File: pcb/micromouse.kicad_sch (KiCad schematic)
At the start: 41 parts, among them J1 B2B-PH-K-S, J12 PINHD_1x5_Female, J15 PINHD_1x2_Female, J2 B2B-PH-K-S, J3 B6B-ZR, J4 B6B-ZR, J7 PINHD_1x5_Female, M1 Left, M2 Right, SW2 SW_DIP_x04, U1 AZ1117-3.3, U2 L293DD, U3 STM32F411RETx, Y1 25 MHz 10 pF, Y2 32.768 kHz 7 pF

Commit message: Add files via upload
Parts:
- J13: renamed from J4; footprint CONN_B6B-ZR_JST -> B6B_ZR:CONN_B6B-ZR_JST
- renumbered C19 to C1, C17 to C10, C20 to C11, C16 to C12, C22 to C16, C5 to C17, C6 to C18, C3 to C19, C12 to C2, C4 to C20, C2 to C21, C1 to C22, C14 to C3, C18 to C4, C13 to C5, C10 to C6, C15 to C7, C11 to C8, C21 to C9, D1 to D3, J2 to J10, J1 to J11, J12 to J6, J15 to J8, J3 to J9, NT2 to NT1, NT1 to NT2, R1 to R?, SW2 to SW1, U3 to U1, U2 to U3, U1 to U4, Y2 to Y1, Y1 to Y2
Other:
- moved on the sheet: C17, C18, C19, C20, J13, J9, M1, M2, NT2, U3

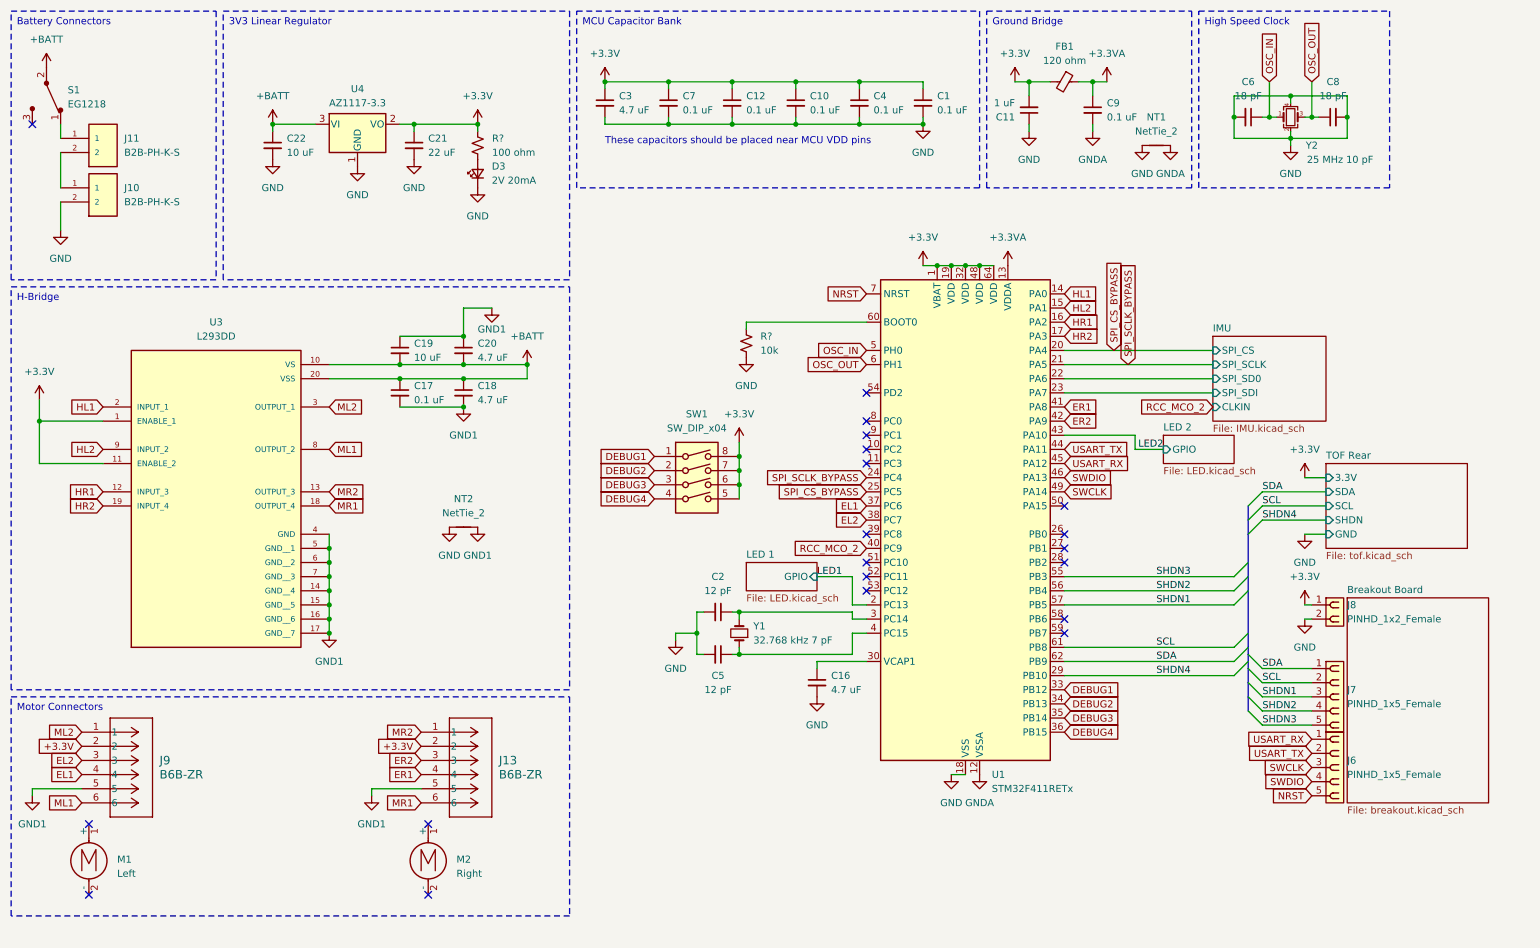
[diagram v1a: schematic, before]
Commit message: Fixed folder structure
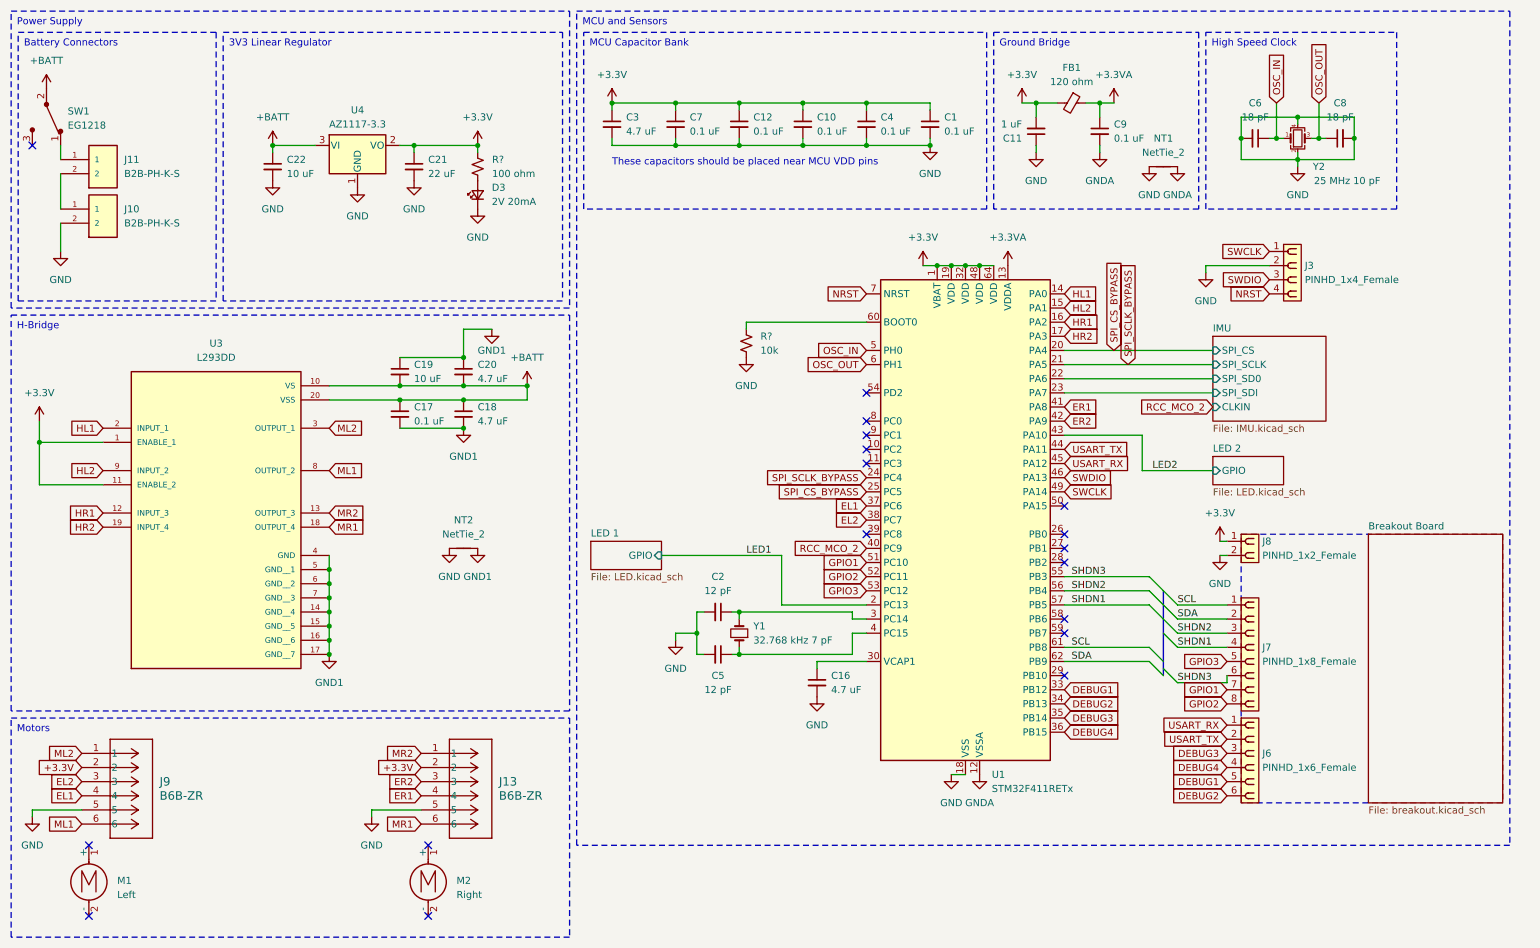
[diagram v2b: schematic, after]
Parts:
- removed J6, J7: PINHD_1x5_Female, Connector_PinSocket_1.00mm:PinSocket_1x05_P1.00mm_Vertical, symbol PCM_SL_Pin_Headers:PINHD_1x5_Female
- removed SW1: SW_DIP_x04, 218-4LPST:218-4LPST, symbol Switch:SW_DIP_x04
- added J3: PINHD_1x4_Female, Connector_PinSocket_2.54mm:PinSocket_1x04_P2.54mm_Vertical, symbol PCM_SL_Pin_Headers:PINHD_1x4_Female
- added J6: PINHD_1x6_Female, Connector_PinSocket_2.54mm:PinSocket_2x03_P2.54mm_Vertical, symbol PCM_SL_Pin_Headers:PINHD_1x6_Female
- added J7: PINHD_1x8_Female, Connector_PinSocket_2.54mm:PinSocket_2x04_P2.54mm_Vertical, symbol PCM_SL_Pin_Headers:PINHD_1x8_Female
- renumbered S1 to SW1
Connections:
- net DEBUG1: now also J6.5
- net DEBUG2: now also J6.6
- net DEBUG3: now also J6.3
- net DEBUG4: now also J6.4
- net GND: now also J13.5, J9.5, J3.2
- net GND1: no longer J13.5, J9.5
- net NRST: now also J3.4
- net SCL: now also J7.1
- net SDA: now also J7.2
- net SHDN1: now also J7.4
- net SHDN2: now also J7.3
- net SHDN3: now also J7.6
- net SWCLK: now also J3.1
- net SWDIO: now also J3.3
- net USART_RX: now also J6.1
- net USART_TX: now also J6.2
- net GPIO1: now reaches U1.51 (PC10)
- net GPIO1: now also J7.7
- net GPIO2: now reaches U1.52 (PC11)
- net GPIO2: now also J7.8
- net GPIO3: now reaches U1.53 (PC12)
- net GPIO3: now also J7.5
- net SHDN4: no longer names the net of U1.29 (PB10)
- no-connect marks 20 -> 18
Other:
- removed sheet TOF Rear
- company: (none) -> UCLA Micromouse 2023-24 Team 2
- title: (none) -> Mouse Potato
- moved on the sheet: C1, C10, C11, C12, C17, C18, C19, C20, C21, C22, C3, C4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

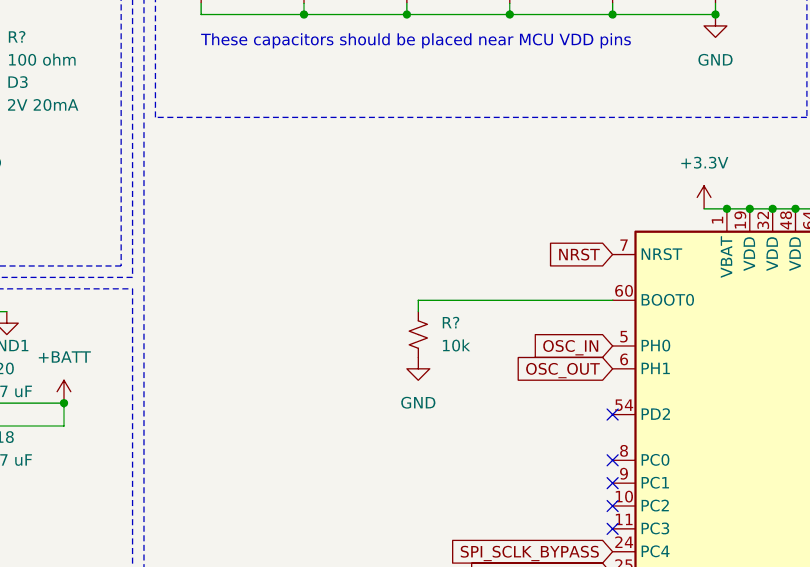
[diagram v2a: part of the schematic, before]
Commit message: added "switch" (jumper)
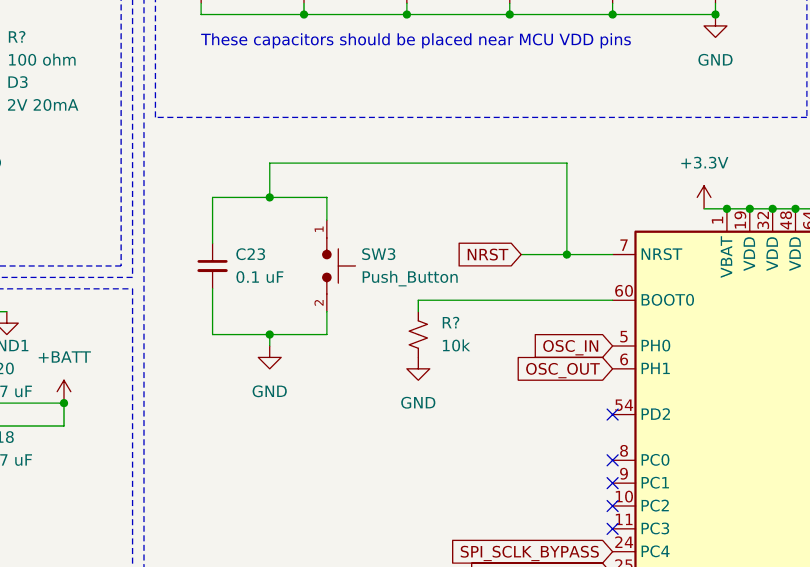
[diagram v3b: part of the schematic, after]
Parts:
- added C23: 0.1 uF, Capacitor_SMD:C_0603_1608Metric, symbol Device:C_Small
- added SW3: Push_Button, Jumper:SolderJumper-2_P1.3mm_Open_Pad1.0x1.5mm, symbol PCM_SL_Devices:Push_Button
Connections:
- net GND: now also C23.2, SW3.2
- net NRST: now also C23.1, SW3.1
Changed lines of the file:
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@@
   (junction (at 209.55 30.48) (diameter 0) (color 0 0 0 0)
   )
+  (junction (at 129.54 58.42) (diameter 0) (color 0 0 0 0)
+  )
   (junction (at 106.68 81.28) (diameter 0) (color 0 0 0 0)
   )
@@
   (junction (at 179.07 38.1) (diameter 0) (color 0 0 0 0)
   )
+  (junction (at 162.56 64.77) (diameter 0) (color 0 0 0 0)
+  )
   (junction (at 255.27 36.83) (diameter 0) (color 0 0 0 0)
   )
@@
   )
   (junction (at 83.82 81.28) (diameter 0) (color 0 0 0 0)
+  )
+  (junction (at 129.54 73.66) (diameter 0) (color 0 0 0 0)
   )
   (junction (at 71.12 116.84) (diameter 0) (color 0 0 0 0)
@@
     (stroke (width 0) (type default))
   )
+  (wire (pts (xy 123.19 73.66) (xy 123.19 68.58))
+    (stroke (width 0) (type default))
+  )
   (wire (pts (xy 144.78 38.1) (xy 144.78 36.83))
     (stroke (width 0) (type default))
@@
     (stroke (width 0) (type default))
   )
+  (wire (pts (xy 162.56 54.61) (xy 162.56 64.77))
+    (stroke (width 0) (type default))
+  )
   (wire (pts (xy 121.92 30.48) (xy 133.35 30.48))
     (stroke (width 0) (type default))
@@
     (stroke (width 0) (type default))
   )
+  (wire (pts (xy 129.54 73.66) (xy 135.89 73.66))
+    (stroke (width 0) (type default))
+  )
   (wire (pts (xy 143.51 121.92) (xy 144.78 121.92))
     (stroke (width 0) (type default))
@@
     (stroke (width 0) (type default))
   )
+  (wire (pts (xy 123.19 58.42) (xy 129.54 58.42))
+    (stroke (width 0) (type default))
+  )
   (wire (pts (xy 71.12 119.38) (xy 71.12 121.92))
     (stroke (width 0) (type default))
@@
     (stroke (width 0) (type default))
   )
+  (wire (pts (xy 135.89 73.66) (xy 135.89 71.12))
+    (stroke (width 0) (type default))
+  )
   (wire (pts (xy 203.2 120.65) (xy 218.44 120.65))
     (stroke (width 0) (type default))
   )
+  (wire (pts (xy 123.19 73.66) (xy 129.54 73.66))
+    (stroke (width 0) (type default))
+  )
   (wire (pts (xy 177.8 59.69) (xy 180.34 59.69))
     (stroke (width 0) (type default))
@@
     (stroke (width 0) (type default))
   )
+  (wire (pts (xy 129.54 58.42) (xy 135.89 58.42))
+    (stroke (width 0) (type default))
+  )
   (wire (pts (xy 203.2 115.57) (xy 218.44 115.57))
     (stroke (width 0) (type default))
   )
+  (wire (pts (xy 129.54 54.61) (xy 129.54 58.42))
+    (stroke (width 0) (type default))
+  )
   (wire (pts (xy 86.36 39.37) (xy 86.36 38.1))
     (stroke (width 0) (type default))
@@
     (stroke (width 0) (type default))
   )
+  (wire (pts (xy 129.54 74.93) (xy 129.54 73.66))
+    (stroke (width 0) (type default))
+  )
   (wire (pts (xy 182.88 151.13) (xy 185.42 151.13))
     (stroke (width 0) (type default))
@@
     (stroke (width 0) (type default))
   )
+  (wire (pts (xy 135.89 58.42) (xy 135.89 60.96))
+    (stroke (width 0) (type default))
+  )
   (wire (pts (xy 182.88 59.69) (xy 185.42 59.69))
     (stroke (width 0) (type default))
@@
     (stroke (width 0) (type default))
   )
+  (wire (pts (xy 157.48 64.77) (xy 162.56 64.77))
+    (stroke (width 0) (type default))
+  )
   (wire (pts (xy 255.27 36.83) (xy 255.27 40.64))
     (stroke (width 0) (type default))
@@
     (stroke (width 0) (type default))
   )
+  (wire (pts (xy 129.54 54.61) (xy 162.56 54.61))
+    (stroke (width 0) (type default))
+  )
   (wire (pts (xy 165.1 129.54) (xy 144.78 129.54))
+    (stroke (width 0) (type default))
+  )
+  (wire (pts (xy 162.56 64.77) (xy 167.64 64.77))
+    (stroke (width 0) (type default))
+  )
+  (wire (pts (xy 123.19 58.42) (xy 123.19 63.5))
     (stroke (width 0) (type default))
   )
@@
     )
   )
-  (global_label "NRST" (shape input) (at 167.64 64.77 180) (fields_autoplaced)
-    (effects (font (size 1.27 1.27)) (justify right))
-    (property "Intersheetrefs" "${INTERSHEET_REFS}" (at 159.8772 64.77 0)
+  (global_label "NRST" (shape input) (at 157.48 64.77 180) (fields_autoplaced)
+    (effects (font (size 1.27 1.27)) (justify right))
+    (property "Intersheetrefs" "${INTERSHEET_REFS}" (at 149.7172 64.77 0)
       (effects (font (size 1.27 1.27)) (justify right) hide)
     )
@@
         (path "/f3ce2b07-9487-48e3-b881-0ad625f4782d"
           (reference "C?") (unit 1)
+        )
+      )
+    )
+  )
+  (symbol (lib_id "power:GND") (at 129.54 74.93 0) (unit 1)
+    (in_bom yes) (on_board yes) (dnp no) (fields_autoplaced)
+    (property "Reference" "#PWR020" (at 129.54 81.28 0)
+      (effects (font (size 1.27 1.27)) hide)
+    )
+    (property "Value" "GND" (at 129.54 80.01 0)
+      (effects (font (size 1.27 1.27)))
+    )
+    (property "Footprint" "" (at 129.54 74.93 0)
+      (effects (font (size 1.27 1.27)) hide)
+    )
+    (property "Datasheet" "" (at 129.54 74.93 0)
+      (effects (font (size 1.27 1.27)) hide)
+    )
+    (pin "1")
+    (instances
+      (project "micromouse"
+        (path "/77cbf270-6b61-4f1a-b1cd-1a823bc4a9d0"
+          (reference "#PWR020") (unit 1)
+        )
+      )
+      (project "button"
+        (path "/91ddd5fd-ed4a-4a3f-ba4e-143f6c4541e0"
+          (reference "#PWR021") (unit 1)
         )
       )
@@
     )
   )
+  (symbol (lib_id "Device:C_Small") (at 123.19 66.04 0) (unit 1)
+    (in_bom yes) (on_board yes) (dnp no) (fields_autoplaced)
+    (property "Reference" "C23" (at 125.73 64.7763 0)
+      (effects (font (size 1.27 1.27)) (justify left))
+    )
+    (property "Value" "0.1 uF" (at 125.73 67.3163 0)
+      (effects (font (size 1.27 1.27)) (justify left))
+    )
+    (property "Footprint" "Capacitor_SMD:C_0603_1608Metric" (at 123.19 66.04 0)
+      (effects (font (size 1.27 1.27)) hide)
+    )
+    (property "Datasheet" "~" (at 123.19 66.04 0)
+      (effects (font (size 1.27 1.27)) hide)
+    )
+    (pin "1")
+    (pin "2")
+    (instances
+      (project "micromouse"
+        (path "/77cbf270-6b61-4f1a-b1cd-1a823bc4a9d0"
+          (reference "C23") (unit 1)
+        )
+      )
+      (project "button"
+        (path "/91ddd5fd-ed4a-4a3f-ba4e-143f6c4541e0"
+          (reference "C15") (unit 1)
+        )
+      )
+    )
+  )
   (symbol (lib_id "power:+3.3V") (at 177.8 59.69 0) (unit 1)
     (in_bom yes) (on_board yes) (dnp no)
@@
         )
       )
+    )
+  )
+  (symbol (lib_id "PCM_SL_Devices:Push_Button") (at 135.89 66.04 270) (unit 1)
+    (in_bom yes) (on_board yes) (dnp no) (fields_autoplaced)
+    (property "Reference" "SW3" (at 139.7 64.77 90)
+      (effects (font (size 1.27 1.27)) (justify left))
+    )
+    (property "Value" "Push_Button" (at 139.7 67.31 90)
+      (effects (font (size 1.27 1.27)) (justify left))
+    )
+    (property "Footprint" "Jumper:SolderJumper-2_P1.3mm_Open_Pad1.0x1.5mm" (at 132.715 65.913 0)
+      (effects (font (size 1.27 1.27)) hide)
+    )
+    (property "Datasheet" "" (at 135.89 66.04 0)
+      (effects (font (size 1.27 1.27)) hide)
+    )
+    (pin "1")
+    (pin "2")
+    (instances
+      (project "micromouse"
+        (path "/77cbf270-6b61-4f1a-b1cd-1a823bc4a9d0"
+          (reference "SW3") (unit 1)
+        )
+      )
+      (project "button"
+        (path "/91ddd5fd-ed4a-4a3f-ba4e-143f6c4541e0"
+          (reference "SW1") (unit 1)
+        )
+      )

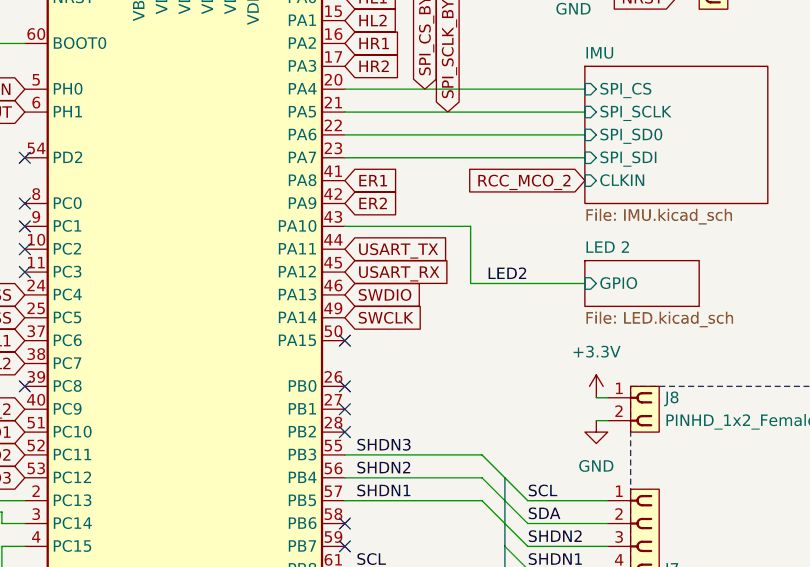
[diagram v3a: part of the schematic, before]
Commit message: added reset jumper to PCB
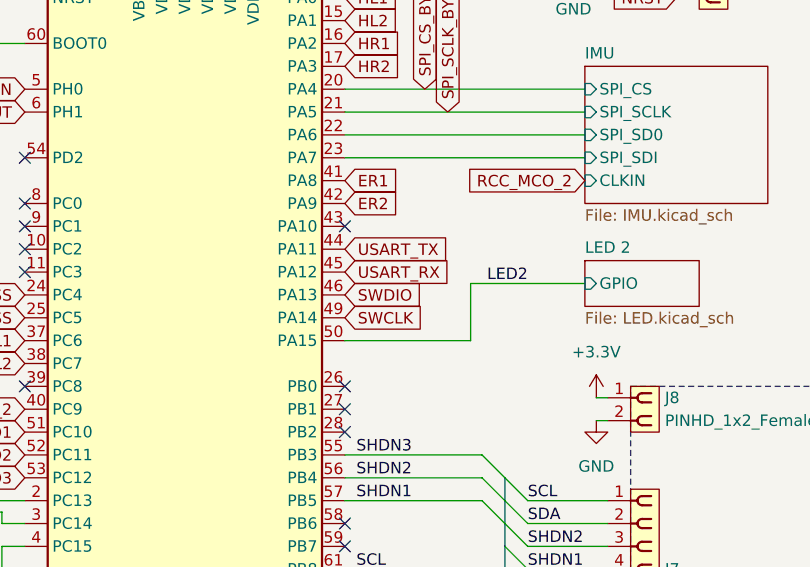
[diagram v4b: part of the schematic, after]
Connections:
- net LED2: now also U1.50 (PA15); no longer U1.43 (PA10)
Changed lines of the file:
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@@
   (no_connect (at 203.2 125.73))
   (no_connect (at 203.2 133.35))
-  (no_connect (at 203.2 102.87))
+  (no_connect (at 203.2 90.17))
   (no_connect (at 88.9 176.53))
   (no_connect (at 167.64 87.63))
@@
     (stroke (width 0) (type default))
   )
-  (wire (pts (xy 217.17 96.52) (xy 217.17 90.17))
+  (wire (pts (xy 217.17 96.52) (xy 217.17 102.87))
     (stroke (width 0) (type default))
   )
@@
     (stroke (width 0) (type default))
   )
-  (wire (pts (xy 217.17 90.17) (xy 203.2 90.17))
-    (stroke (width 0) (type default))
-  )
   (wire (pts (xy 203.2 82.55) (xy 229.87 82.55))
     (stroke (width 0) (type default))
@@
     (stroke (width 0) (type default))
   )
+  (wire (pts (xy 217.17 102.87) (xy 203.2 102.87))
+    (stroke (width 0) (type default))
+  )
